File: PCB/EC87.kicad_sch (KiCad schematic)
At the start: 29 parts, among them J1 SW Debug, SW1 BOOT0, SW89 Reset, U1 STM32F411CEUx, U5 XC6206PxxxMR, Y1 8MHz

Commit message: Update
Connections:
- net AMUX_SEL_0: now also U1.18 (PB0); no longer U1.17 (PA7)
- net AMUX_SEL_1: now also U1.17 (PA7); no longer U1.16 (PA6)
- net AMUX_SEL_2: now also U1.16 (PA6); no longer U1.15 (PA5)
- net APLEX_EN_PIN_0: now also U1.26 (PB13); no longer U1.18 (PB0)
- new net DISCHARGE_PIN: U1.15 (PA5)
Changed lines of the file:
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@@
+    )
+  )
+  (global_label "APLEX_EN_PIN_0" (shape input) (at 83.82 135.89 180) (fields_autoplaced)
+    (effects (font (size 1.27 1.27)) (justify right))
+    (property "Intersheet References" "${INTERSHEET_REFS}" (id 0) (at 65.8645 135.8106 0)
+      (effects (font (size 1.27 1.27)) (justify right) hide)
     )
   )
@@
     )
   )
+  (global_label "AMUX_SEL_0" (shape input) (at 83.82 105.41 180) (fields_autoplaced)
+    (effects (font (size 1.27 1.27)) (justify right))
+    (property "Intersheet References" "${INTERSHEET_REFS}" (id 0) (at 69.7955 105.3306 0)
+      (effects (font (size 1.27 1.27)) (justify right) hide)
+    )
+  )
   (global_label "VDD2" (shape input) (at 101.6 63.5 90) (fields_autoplaced)
     (effects (font (size 1.27 1.27)) (justify left))
@@
     )
   )
-  (global_label "APLEX_EN_PIN_0" (shape input) (at 83.82 105.41 180) (fields_autoplaced)
-    (effects (font (size 1.27 1.27)) (justify right))
-    (property "Intersheet References" "${INTERSHEET_REFS}" (id 0) (at 65.8645 105.3306 0)
-      (effects (font (size 1.27 1.27)) (justify right) hide)
-    )
-  )
   (global_label "BOOT0" (shape input) (at 50.8 177.8 0) (fields_autoplaced)
     (effects (font (size 1.27 1.27)) (justify left))
@@
     )
   )
+  (global_label "DISCHARGE_PIN" (shape input) (at 120.65 115.57 0) (fields_autoplaced)
+    (effects (font (size 1.27 1.27)) (justify left))
+    (property "Intersheet References" "${INTERSHEET_REFS}" (id 0) (at 137.6983 115.4906 0)
+      (effects (font (size 1.27 1.27)) (justify left) hide)
+    )
+  )
   (global_label "D+" (shape input) (at 40.64 41.91 0) (fields_autoplaced)
     (effects (font (size 1.27 1.27)) (justify left))
@@
     )
   )
-  (global_label "AMUX_SEL_2" (shape input) (at 120.65 115.57 0) (fields_autoplaced)
-    (effects (font (size 1.27 1.27)) (justify left))
-    (property "Intersheet References" "${INTERSHEET_REFS}" (id 0) (at 134.6745 115.6494 0)
-      (effects (font (size 1.27 1.27)) (justify left) hide)
-    )
-  )
   (global_label "D-" (shape input) (at 40.64 39.37 0) (fields_autoplaced)
     (effects (font (size 1.27 1.27)) (justify left))
@@
     )
   )
+  (global_label "AMUX_SEL_2" (shape input) (at 120.65 118.11 0) (fields_autoplaced)
+    (effects (font (size 1.27 1.27)) (justify left))
+    (property "Intersheet References" "${INTERSHEET_REFS}" (id 0) (at 134.6745 118.1894 0)
+      (effects (font (size 1.27 1.27)) (justify left) hide)
+    )
+  )
   (global_label "XTAL0" (shape input) (at 163.83 83.82 90) (fields_autoplaced)
     (effects (font (size 1.27 1.27)) (justify left))
@@
     )
   )
-  (global_label "AMUX_SEL_0" (shape input) (at 120.65 120.65 0) (fields_autoplaced)
+  (global_label "VBAT" (shape input) (at 93.98 177.8 0) (fields_autoplaced)
+    (effects (font (size 1.27 1.27)) (justify left))
+    (property "Intersheet References" "${INTERSHEET_REFS}" (id 0) (at 100.8079 177.7206 0)
+      (effects (font (size 1.27 1.27)) (justify left) hide)
+    )
+  )
+  (global_label "SWCLK" (shape input) (at 22.86 143.51 180) (fields_autoplaced)
+    (effects (font (size 1.27 1.27)) (justify right))
+    (property "Intersheet References" "${INTERSHEET_REFS}" (id 0) (at 14.2179 143.5894 0)
+      (effects (font (size 1.27 1.27)) (justify right) hide)
+    )
+  )
+  (global_label "ROW3" (shape input) (at 80.01 113.03 180) (fields_autoplaced)
+    (effects (font (size 1.27 1.27)) (justify right))
+    (property "Intersheet References" "${INTERSHEET_REFS}" (id 0) (at 72.3355 112.9506 0)
+      (effects (font (size 1.27 1.27)) (justify right) hide)
+    )
+  )
+  (global_label "ROW0" (shape input) (at 80.01 115.57 180) (fields_autoplaced)
+    (effects (font (size 1.27 1.27)) (justify right))
+    (property "Intersheet References" "${INTERSHEET_REFS}" (id 0) (at 72.3355 115.6494 0)
+      (effects (font (size 1.27 1.27)) (justify right) hide)
+    )
+  )
+  (global_label "D-" (shape input) (at 149.86 33.02 0) (fields_autoplaced)
+    (effects (font (size 1.27 1.27)) (justify left))
+    (property "Intersheet References" "${INTERSHEET_REFS}" (id 0) (at 155.1155 32.9406 0)
+      (effects (font (size 1.27 1.27)) (justify left) hide)
+    )
+  )
+  (global_label "ROW1" (shape input) (at 129.54 138.43 0) (fields_autoplaced)
+    (effects (font (size 1.27 1.27)) (justify left))
+    (property "Intersheet References" "${INTERSHEET_REFS}" (id 0) (at 137.2145 138.3506 0)
+      (effects (font (size 1.27 1.27)) (justify left) hide)
+    )
+  )
+  (global_label "AMUX_SEL_1" (shape input) (at 120.65 120.65 0) (fields_autoplaced)
     (effects (font (size 1.27 1.27)) (justify left))
     (property "Intersheet References" "${INTERSHEET_REFS}" (id 0) (at 134.6745 120.7294 0)
@@
     )
   )
-  (global_label "VBAT" (shape input) (at 93.98 177.8 0) (fields_autoplaced)
-    (effects (font (size 1.27 1.27)) (justify left))
-    (property "Intersheet References" "${INTERSHEET_REFS}" (id 0) (at 100.8079 177.7206 0)
-      (effects (font (size 1.27 1.27)) (justify left) hide)
-    )
-  )
-  (global_label "SWCLK" (shape input) (at 22.86 143.51 180) (fields_autoplaced)
-    (effects (font (size 1.27 1.27)) (justify right))
-    (property "Intersheet References" "${INTERSHEET_REFS}" (id 0) (at 14.2179 143.5894 0)
-      (effects (font (size 1.27 1.27)) (justify right) hide)
-    )
-  )
-  (global_label "ROW3" (shape input) (at 80.01 113.03 180) (fields_autoplaced)
-    (effects (font (size 1.27 1.27)) (justify right))
-    (property "Intersheet References" "${INTERSHEET_REFS}" (id 0) (at 72.3355 112.9506 0)
-      (effects (font (size 1.27 1.27)) (justify right) hide)
-    )
-  )
-  (global_label "ROW0" (shape input) (at 80.01 115.57 180) (fields_autoplaced)
-    (effects (font (size 1.27 1.27)) (justify right))
-    (property "Intersheet References" "${INTERSHEET_REFS}" (id 0) (at 72.3355 115.6494 0)
-      (effects (font (size 1.27 1.27)) (justify right) hide)
-    )
-  )
-  (global_label "D-" (shape input) (at 149.86 33.02 0) (fields_autoplaced)
-    (effects (font (size 1.27 1.27)) (justify left))
-    (property "Intersheet References" "${INTERSHEET_REFS}" (id 0) (at 155.1155 32.9406 0)
-      (effects (font (size 1.27 1.27)) (justify left) hide)
-    )
-  )
-  (global_label "ROW1" (shape input) (at 129.54 138.43 0) (fields_autoplaced)
-    (effects (font (size 1.27 1.27)) (justify left))
-    (property "Intersheet References" "${INTERSHEET_REFS}" (id 0) (at 137.2145 138.3506 0)
-      (effects (font (size 1.27 1.27)) (justify left) hide)
-    )
-  )
   (global_label "VDDA" (shape input) (at 106.68 63.5 90) (fields_autoplaced)
     (effects (font (size 1.27 1.27)) (justify left))
@@
       (effects (font (size 1.27 1.27)) (justify left) hide)
     )
-  )
-  (global_label "AMUX_SEL_1" (shape input) (at 120.65 118.11 0) (fields_autoplaced)
-    (effects (font (size 1.27 1.27)) (justify left))
-    (property "Intersheet References" "${INTERSHEET_REFS}" (id 0) (at 134.6745 118.1894 0)
-      (effects (font (size 1.27 1.27)) (justify left) hide)
-    )

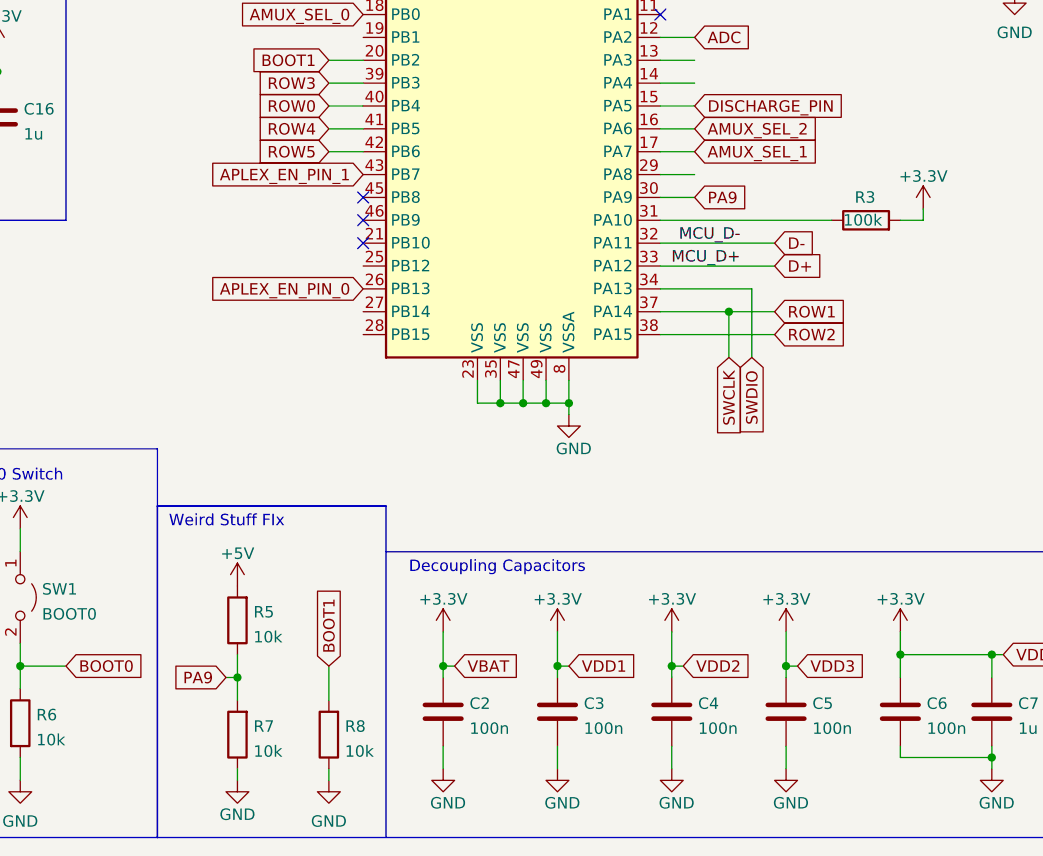
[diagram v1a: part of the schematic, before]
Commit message: Update final schematic and PCB
PCB and schematic are finalized, now proceeding to addition of GND vias to shield from parasitic capacitance.
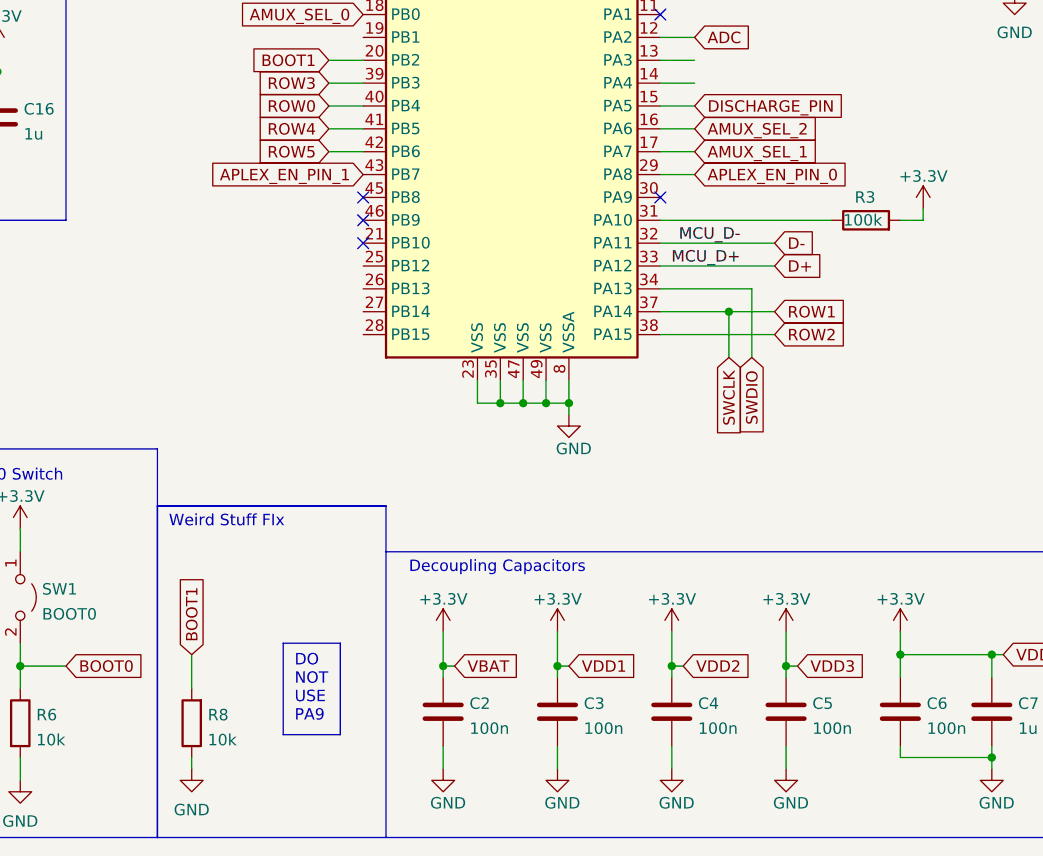
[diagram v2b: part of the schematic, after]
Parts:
- removed R5, R7: 10k, Resistor_SMD:R_0603_1608Metric, symbol Device:R
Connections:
- net APLEX_EN_PIN_0: now also U1.29 (PA8); no longer U1.26 (PB13)
- net PA9: no longer names the net of U1.30 (PA9)
- no-connect marks 10 -> 11
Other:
- note added: "DO NOT USE PA9"
- moved on the sheet: R8
